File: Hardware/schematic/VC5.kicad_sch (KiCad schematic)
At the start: 2 parts, among them J2 Debug_output

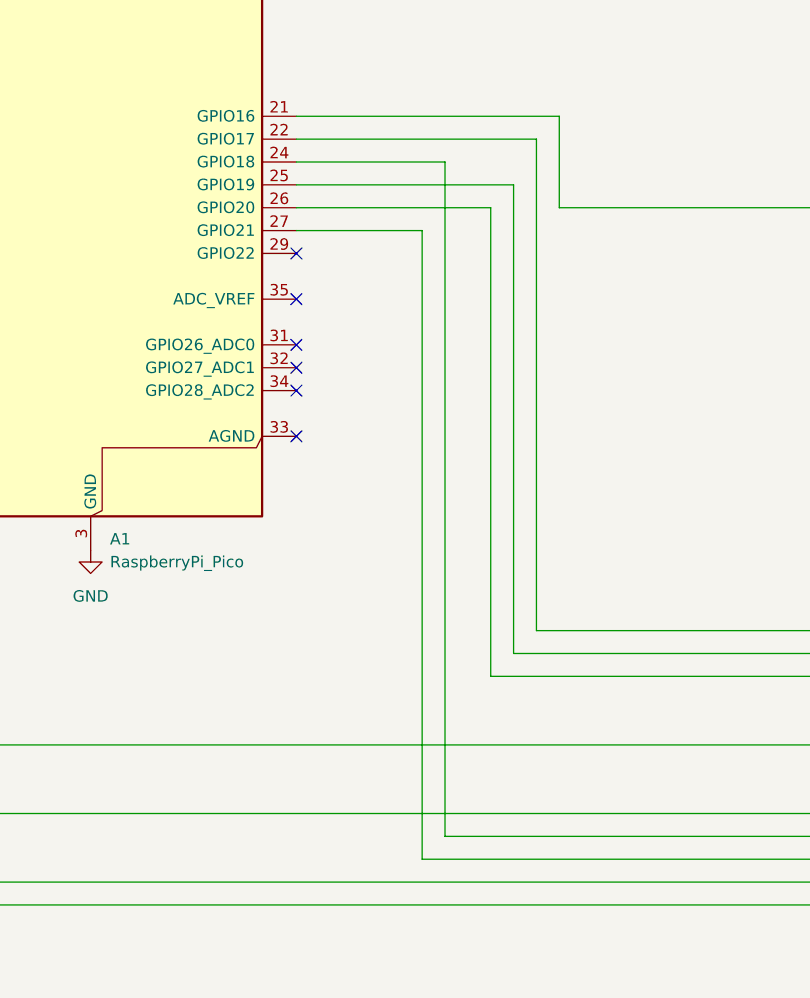
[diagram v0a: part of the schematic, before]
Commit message: fixed mistake in the schematic
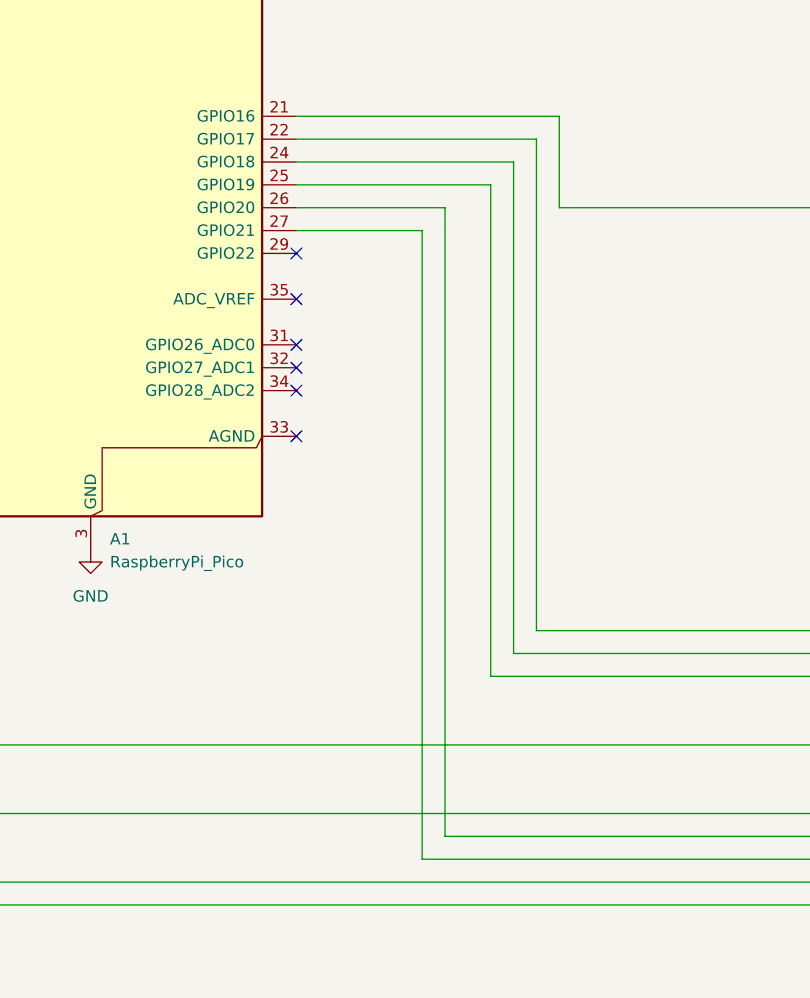
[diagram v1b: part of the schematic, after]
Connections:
- net displays/CLK: now also A1.24 (GPIO18); no longer A1.25 (GPIO19)
- net displays/CS1: now also A1.26 (GPIO20); no longer A1.24 (GPIO18)
- net displays/DIN: now also A1.25 (GPIO19); no longer A1.26 (GPIO20)
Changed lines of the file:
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@@
-	(wire
-		(pts
-			(xy 200.66 118.11) (xy 200.66 66.04)
-		)
-		(stroke
-			(width 0)
-			(type default)
-		)
-	)
 	(wire
 		(pts
@@
 	(wire
 		(pts
-			(xy 193.04 63.5) (xy 193.04 138.43)
-		)
-		(stroke
-			(width 0)
-			(type default)
-		)
-	)
-	(wire
-		(pts
-			(xy 198.12 120.65) (xy 198.12 68.58)
+			(xy 193.04 68.58) (xy 193.04 138.43)
 		)
 		(stroke
@@
 	(wire
 		(pts
+			(xy 198.12 120.65) (xy 198.12 66.04)
+		)
+		(stroke
+			(width 0)
+			(type default)
+		)
+	)
+	(wire
+		(pts
 			(xy 123.19 91.44) (xy 130.81 91.44)
 		)
@@
 	(wire
 		(pts
-			(xy 176.53 66.04) (xy 200.66 66.04)
-		)
-		(stroke
-			(width 0)
-			(type default)
-		)
-	)
-	(wire
-		(pts
 			(xy 200.66 118.11) (xy 233.68 118.11)
 		)
@@
 	(wire
 		(pts
+			(xy 200.66 63.5) (xy 200.66 118.11)
+		)
+		(stroke
+			(width 0)
+			(type default)
+		)
+	)
+	(wire
+		(pts
+			(xy 198.12 66.04) (xy 176.53 66.04)
+		)
+		(stroke
+			(width 0)
+			(type default)
+		)
+	)
+	(wire
+		(pts
 			(xy 205.74 58.42) (xy 176.53 58.42)
 		)
@@
 	(wire
 		(pts
+			(xy 176.53 68.58) (xy 193.04 68.58)
+		)
+		(stroke
+			(width 0)
+			(type default)
+		)
+	)
+	(wire
+		(pts
 			(xy 115.57 128.27) (xy 233.68 128.27)
 		)
@@
 	(wire
 		(pts
-			(xy 176.53 63.5) (xy 193.04 63.5)
-		)
-		(stroke
-			(width 0)
-			(type default)
-		)
-	)
-	(wire
-		(pts
 			(xy 59.69 71.12) (xy 130.81 71.12)
 		)
@@
 	(wire
 		(pts
-			(xy 176.53 68.58) (xy 198.12 68.58)
-		)
-		(stroke
-			(width 0)
-			(type default)
-		)
-	)
-	(wire
-		(pts
 			(xy 205.74 68.58) (xy 205.74 58.42)
 		)
@@
 		)
 		(stroke
+			(width 0)
+			(type default)
+		)
+	)
+	(wire
+		(pts
+			(xy 176.53 63.5) (xy 200.66 63.5)
+		)
+		(stroke
